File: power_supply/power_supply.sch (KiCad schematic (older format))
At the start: 50 parts, among them J1 Conn_01x04_Male, J2 Conn_01x03_Male, J3 Conn_01x03_Male, J4 Conn_01x03_Male, J5 Conn_01x02_Male, U1 LM7815_TO220, U2 LM7915_TO220, U3 LM7815_TO220

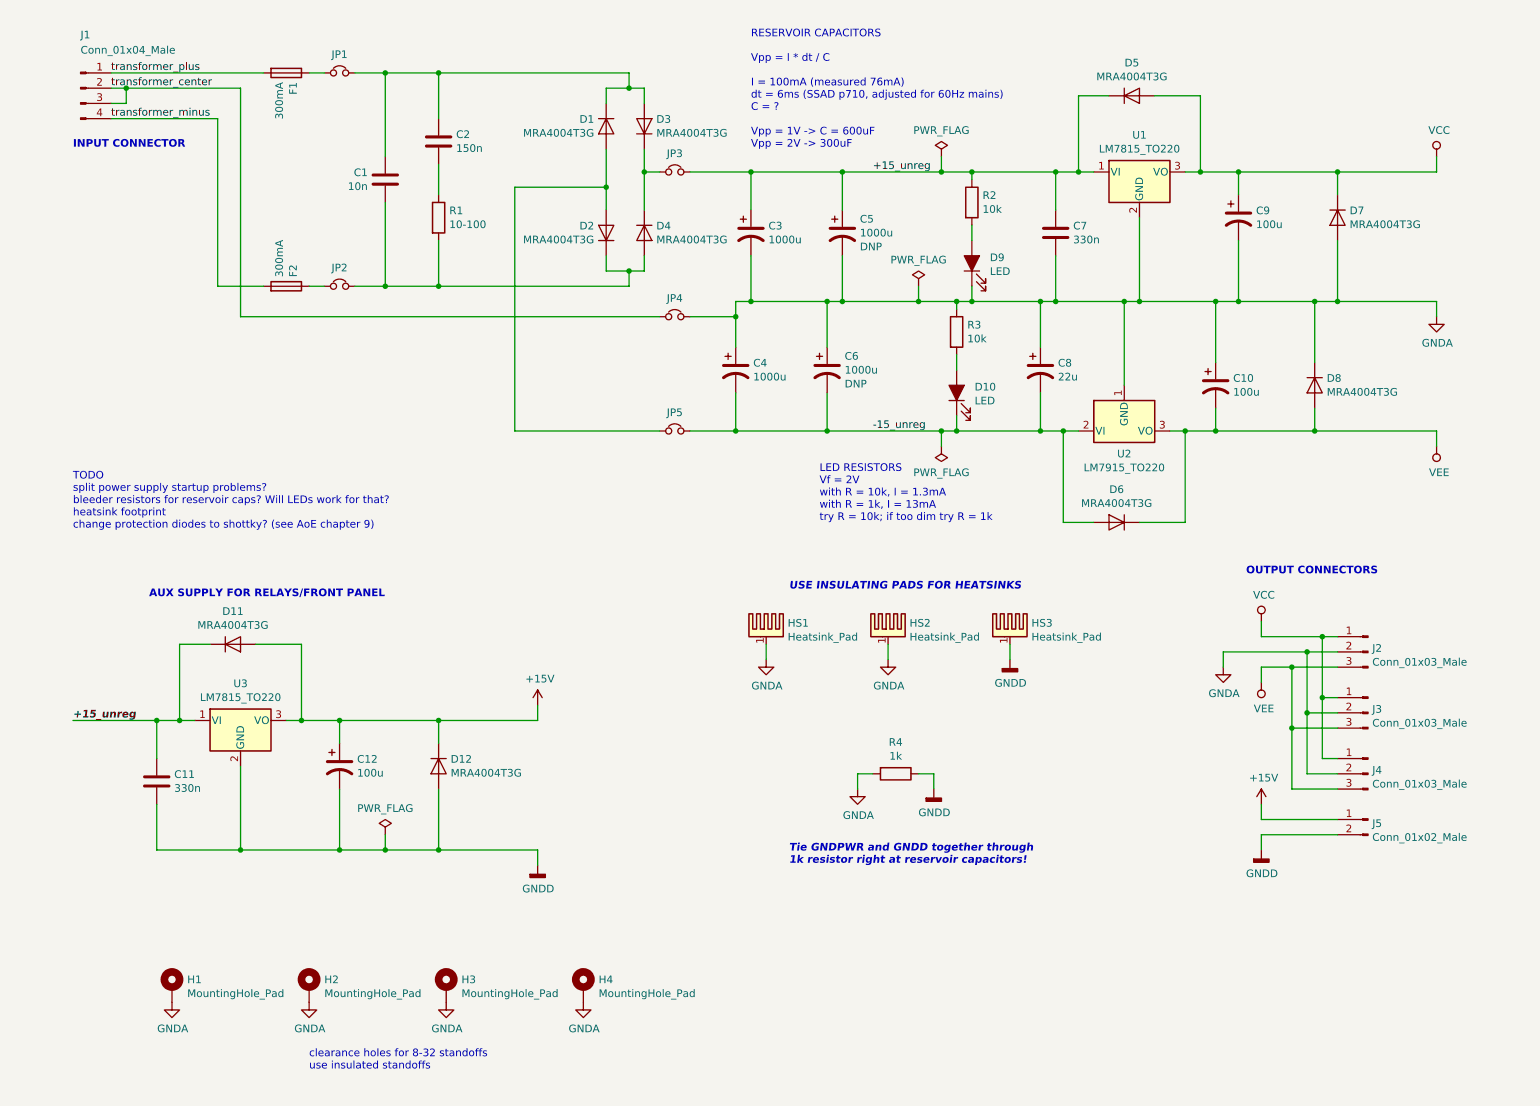
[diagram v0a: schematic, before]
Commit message: update power symbols (add relay power&ground)
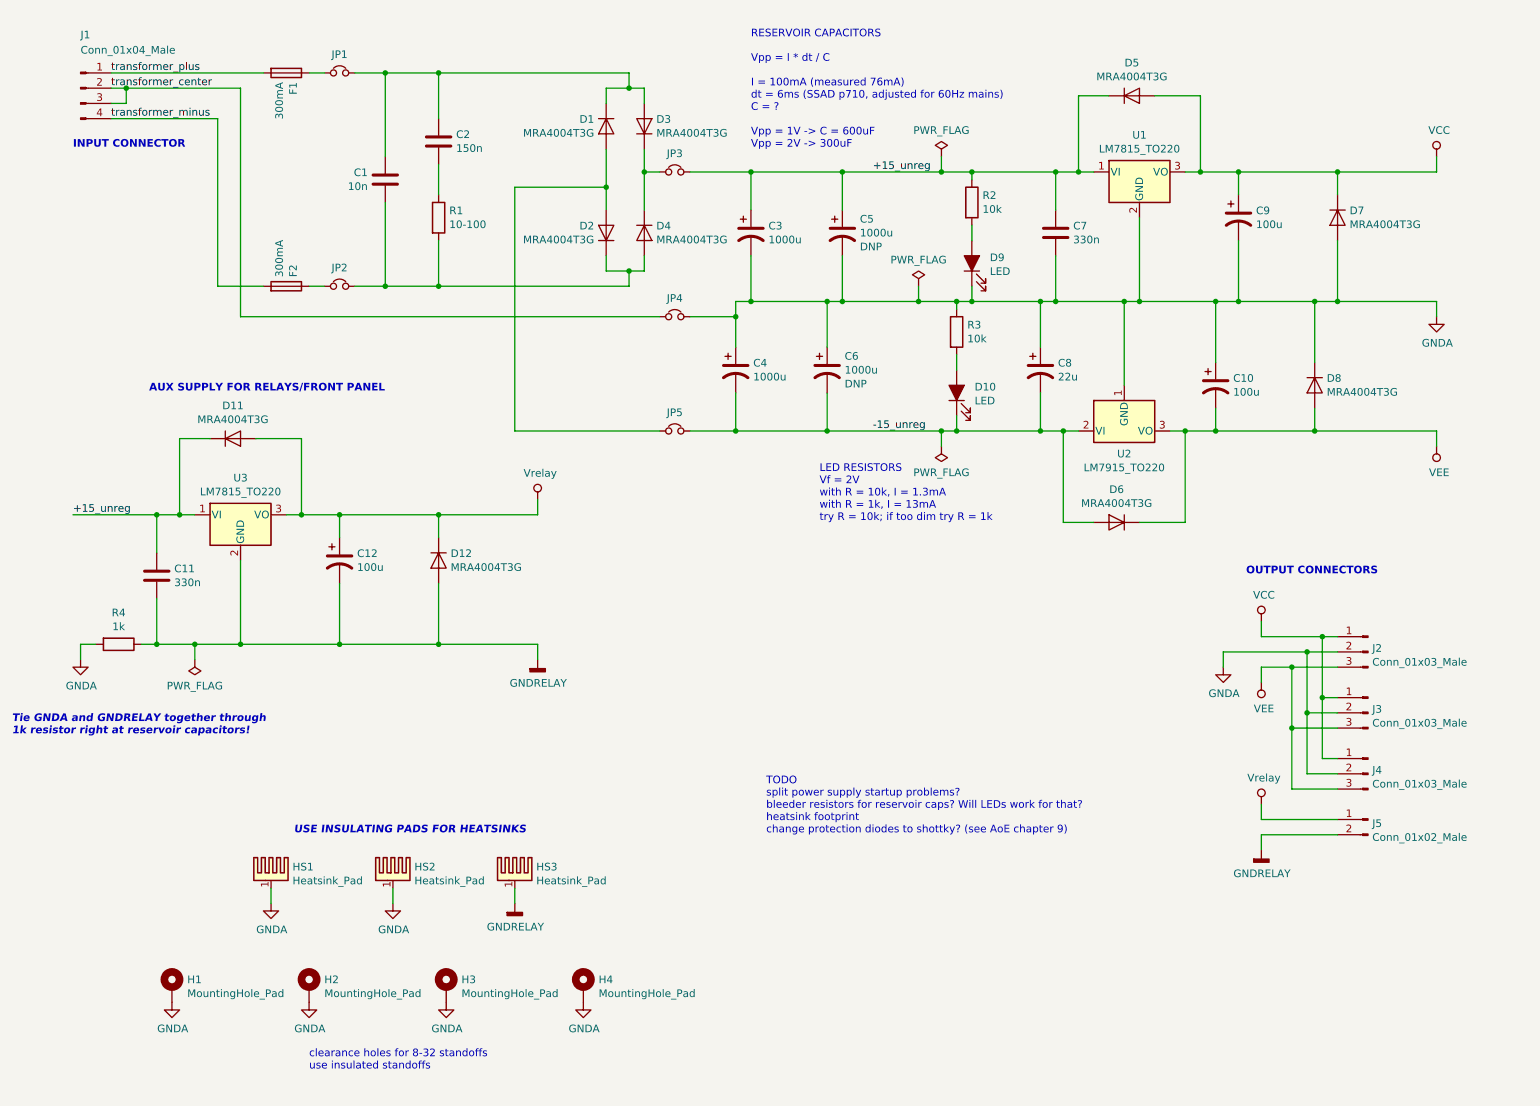
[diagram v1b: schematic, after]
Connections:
- net +15V renamed Vrelay
- net GNDD renamed GNDRELAY
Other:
- note added: "Tie GNDA and GNDRELAY together through\n1k resistor right at reservoir capacitors!"
- note removed: "Tie GNDPWR and GNDD together through\n1k resistor right at reservoir capacitors!"
- moved on the sheet: C11, C12, D11, D12, HS1, HS2, HS3, R4, U3

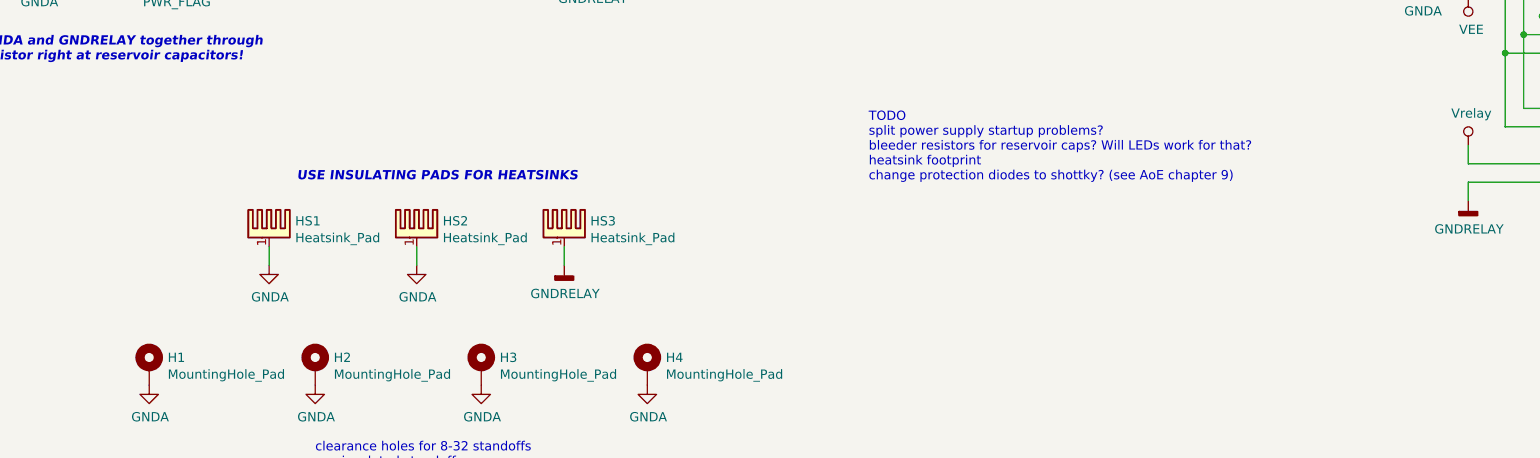
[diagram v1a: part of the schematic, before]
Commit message: update heatsinks in schematic
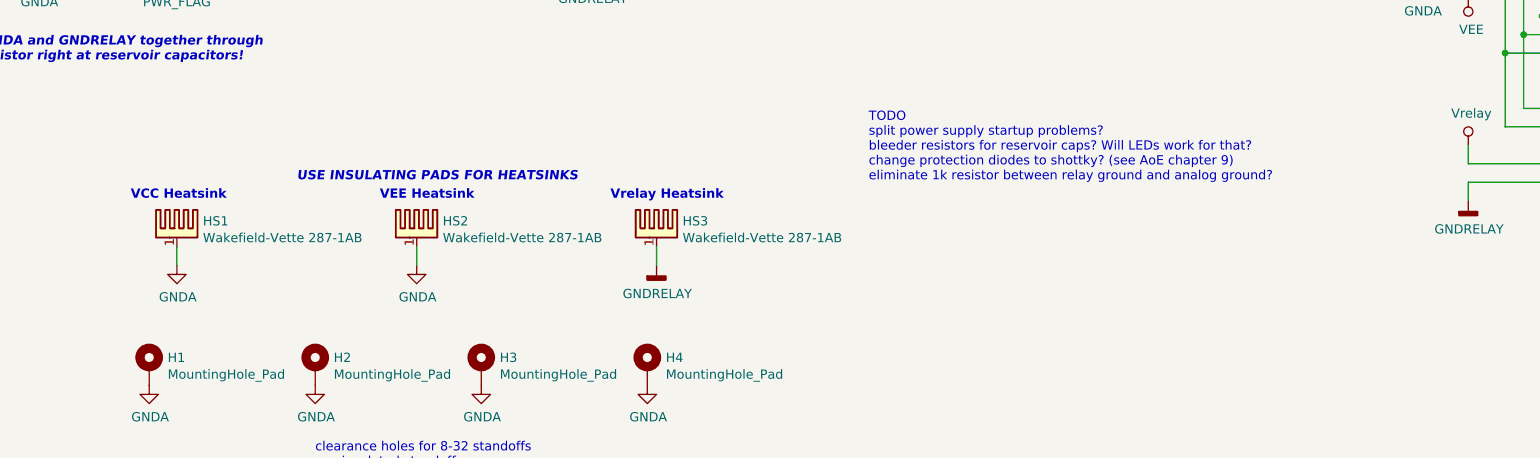
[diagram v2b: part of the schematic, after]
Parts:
- HS1, HS2, HS3: value Heatsink_Pad -> Wakefield-Vette 287-1AB; footprint Heatsink:Heatsink_35x26mm_1xFixation3mm_Fischer-SK486-35 -> Heatsink_gkeeth:Heatsink_Wakefield-Vette_287-1AB_T0-220_Vertical
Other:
- note added: "TODO\nsplit power supply startup problems?\nbleeder resistors for reservoir caps? Will LEDs work for that?\nchange protection diodes to shottky? (see AoE chapter 9)\neliminate 1k resistor between relay ground and analog ground?"
- note added: "VCC Heatsink"
- note added: "VEE Heatsink"
- note added: "Vrelay Heatsink"
- note removed: "TODO\nsplit power supply startup problems?\nbleeder resistors for reservoir caps? Will LEDs work for that?\nheatsink footprint\nchange protection diodes to shottky? (see AoE chapter 9)"
- moved on the sheet: HS1, HS3
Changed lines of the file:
@@
 $EndComp
 Text Notes 5500 6250 0    50   ~ 0
-TODO\nsplit power supply startup problems?\nbleeder resistors for reservoir caps? Will LEDs work for that?\nheatsink footprint\nchange protection diodes to shottky? (see AoE chapter 9)
+TODO\nsplit power supply startup problems?\nbleeder resistors for reservoir caps? Will LEDs work for that?\nchange protection diodes to shottky? (see AoE chapter 9)\neliminate 1k resistor between relay ground and analog ground?
 $Comp
 L Device:CP1 C8
@@
 $EndComp
 $Comp
-L Mechanical:Heatsink_Pad HS1
-U 1 1 5CB4FC2E
-P 2250 6500
-F 0 "HS1" H 2391 6539 50  0000 L CNN
-F 1 "Heatsink_Pad" H 2391 6448 50  0000 L CNN
-F 2 "Heatsink:Heatsink_35x26mm_1xFixation3mm_Fischer-SK486-35" H 2262 6450 50  0001 C CNN
-F 3 "~" H 2262 6450 50  0001 C CNN
-	1    2250 6500
-	1    0    0    -1
-$EndComp
-$Comp
 L Mechanical:Heatsink_Pad HS2
 U 1 1 5CB5054C
 P 3050 6500
 F 0 "HS2" H 3191 6539 50  0000 L CNN
-F 1 "Heatsink_Pad" H 3191 6448 50  0000 L CNN
-F 2 "Heatsink:Heatsink_35x26mm_1xFixation3mm_Fischer-SK486-35" H 3062 6450 50  0001 C CNN
+F 1 "Wakefield-Vette 287-1AB" H 3191 6448 50  0000 L CNN
+F 2 "Heatsink_gkeeth:Heatsink_Wakefield-Vette_287-1AB_T0-220_Vertical" H 3062 6450 50  0001 C CNN
 F 3 "~" H 3062 6450 50  0001 C CNN
 	1    3050 6500
@@
 Wire Wire Line
 	3050 6600 3050 6700
-Wire Wire Line
-	2250 6600 2250 6700
 Text Notes 2400 6250 0    50   Italic 10
 USE INSULATING PADS FOR HEATSINKS
@@
 	4000 4150 4000 4050
 $Comp
-L power:GNDA #PWR0106
-U 1 1 5CFBDF10
-P 2250 6700
-F 0 "#PWR0106" H 2250 6450 50  0001 C CNN
-F 1 "GNDA" H 2255 6527 50  0000 C CNN
-F 2 "" H 2250 6700 50  0001 C CNN
-F 3 "" H 2250 6700 50  0001 C CNN
-	1    2250 6700
-	1    0    0    -1
-$EndComp
-$Comp
 L power:GNDA #PWR0107
 U 1 1 5CFBE3DC
@@
 L Mechanical:Heatsink_Pad HS3
 U 1 1 5CFC037A
-P 3850 6500
-F 0 "HS3" H 3991 6539 50  0000 L CNN
-F 1 "Heatsink_Pad" H 3991 6448 50  0000 L CNN
-F 2 "Heatsink:Heatsink_35x26mm_1xFixation3mm_Fischer-SK486-35" H 3862 6450 50  0001 C CNN
-F 3 "~" H 3862 6450 50  0001 C CNN
-	1    3850 6500
-	1    0    0    -1
-$EndComp
-Wire Wire Line
-	3850 6600 3850 6700
+P 4350 6500
+F 0 "HS3" H 4491 6539 50  0000 L CNN
+F 1 "Wakefield-Vette 287-1AB" H 4491 6448 50  0000 L CNN
+F 2 "Heatsink_gkeeth:Heatsink_Wakefield-Vette_287-1AB_T0-220_Vertical" H 4362 6450 50  0001 C CNN
+F 3 "~" H 4362 6450 50  0001 C CNN
+	1    4350 6500
+	1    0    0    -1
+$EndComp
+Wire Wire Line
+	4350 6600 4350 6700
 $Comp
 L Connector:Conn_01x02_Male J5
@@
 L power_gkeeth:GNDRELAY #PWR0117
 U 1 1 5CCD5AC4
-P 3850 6700
-F 0 "#PWR0117" H 3850 6450 50  0001 C CNN
-F 1 "GNDRELAY" H 3854 6545 50  0000 C CNN
-F 2 "" H 3850 6700 50  0001 C CNN
-F 3 "" H 3850 6700 50  0001 C CNN
-	1    3850 6700
+P 4350 6700
+F 0 "#PWR0117" H 4350 6450 50  0001 C CNN
+F 1 "GNDRELAY" H 4354 6545 50  0000 C CNN
+F 2 "" H 4350 6700 50  0001 C CNN
+F 3 "" H 4350 6700 50  0001 C CNN
+	1    4350 6700
 	1    0    0    -1
 $EndComp
@@
 Wire Wire Line
 	1750 5000 1500 5000
+$Comp
+L power:GNDA #PWR0106
+U 1 1 5CFBDF10
+P 1750 6700
+F 0 "#PWR0106" H 1750 6450 50  0001 C CNN
+F 1 "GNDA" H 1755 6527 50  0000 C CNN
+F 2 "" H 1750 6700 50  0001 C CNN
+F 3 "" H 1750 6700 50  0001 C CNN
+	1    1750 6700
+	1    0    0    -1
+$EndComp
+Wire Wire Line
+	1750 6600 1750 6700
+$Comp
+L Mechanical:Heatsink_Pad HS1
+U 1 1 5CB4FC2E
+P 1750 6500
+F 0 "HS1" H 1891 6539 50  0000 L CNN
+F 1 "Wakefield-Vette 287-1AB" H 1891 6448 50  0000 L CNN
+F 2 "Heatsink_gkeeth:Heatsink_Wakefield-Vette_287-1AB_T0-220_Vertical" H 1762 6450 50  0001 C CNN
+F 3 "~" H 1762 6450 50  0001 C CNN
+	1    1750 6500
+	1    0    0    -1
+$EndComp
+Text Notes 1500 6350 0    50   ~ 10
+VCC Heatsink
+Text Notes 2850 6350 0    50   ~ 10
+VEE Heatsink
+Text Notes 4100 6350 0    50   ~ 10
+Vrelay Heatsink
 $EndSCHEMATC

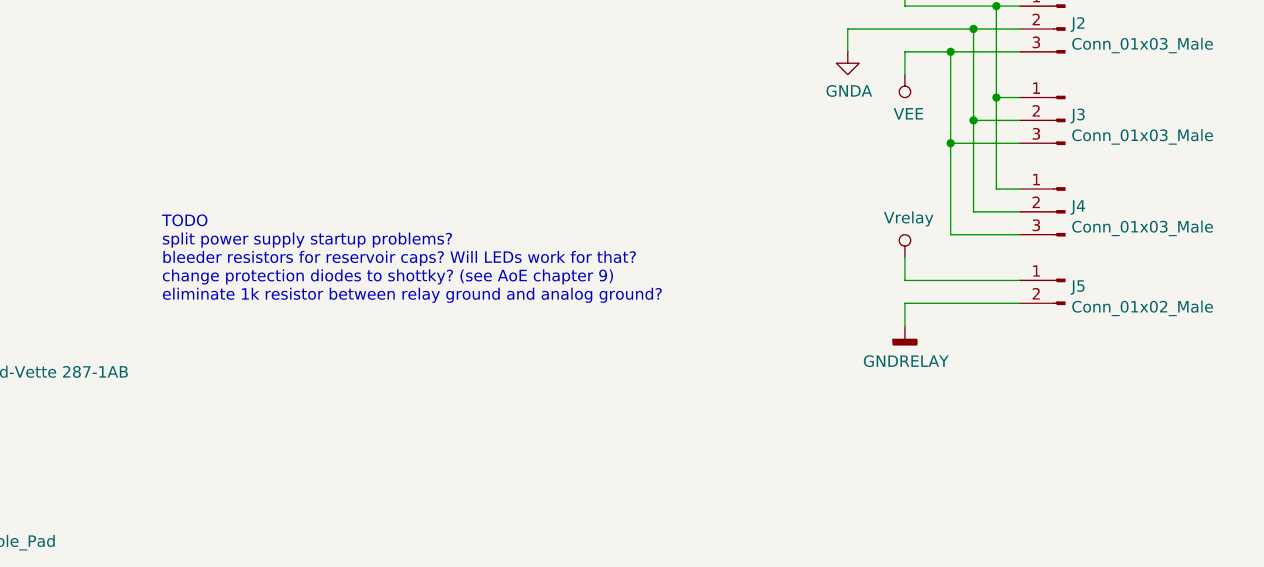
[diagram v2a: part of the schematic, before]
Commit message: update TODO and add extra connector for relay power
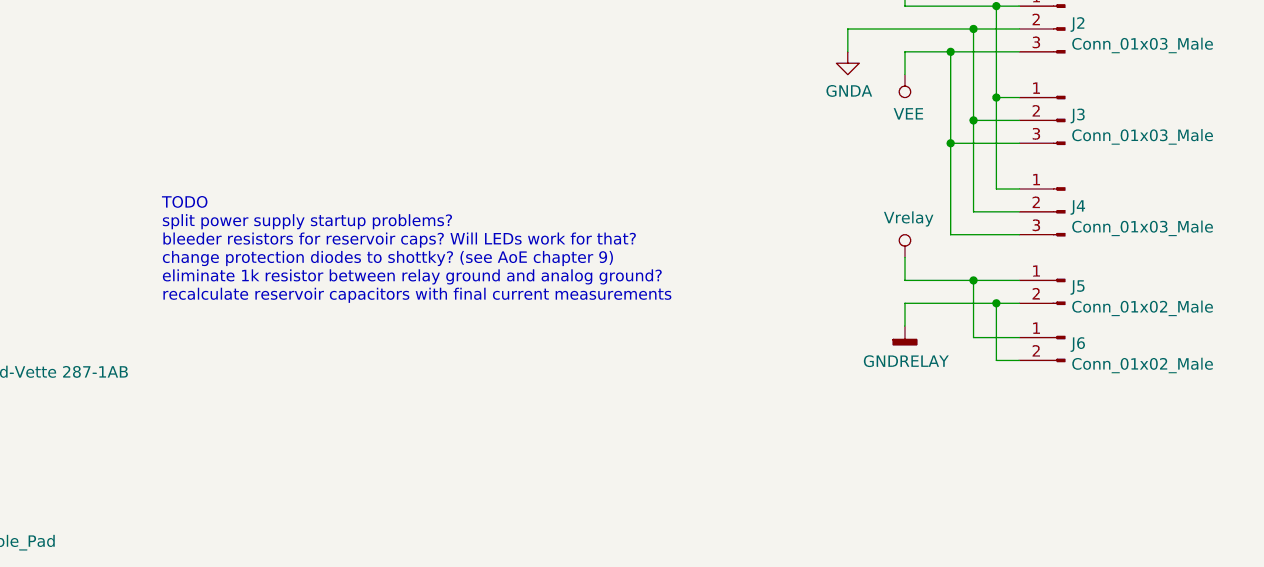
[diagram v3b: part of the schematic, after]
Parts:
- added J6: Conn_01x02_Male, Connector_Molex_SL:Molex_SL_A-70543-0001_1x02_P2.54mm_Vertical, symbol Connector:Conn_01x02_Male
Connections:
- net GNDRELAY: now also J6.2 (Pin_2)
- net Vrelay: now also J6.1 (Pin_1)
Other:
- note added: "TODO\nsplit power supply startup problems?\nbleeder resistors for reservoir caps? Will LEDs work for that?\nchange protection diodes to shottky? (see AoE chapter 9)\neliminate 1k resistor between relay ground and analog ground?\nrecalculate reservoir capacitors with final current measurements"
- note removed: "TODO\nsplit power supply startup problems?\nbleeder resistors for reservoir caps? Will LEDs work for that?\nchange protection diodes to shottky? (see AoE chapter 9)\neliminate 1k resistor between relay ground and analog ground?"
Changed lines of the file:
@@
 $EndComp
 Text Notes 5500 6250 0    50   ~ 0
-TODO\nsplit power supply startup problems?\nbleeder resistors for reservoir caps? Will LEDs work for that?\nchange protection diodes to shottky? (see AoE chapter 9)\neliminate 1k resistor between relay ground and analog ground?
+TODO\nsplit power supply startup problems?\nbleeder resistors for reservoir caps? Will LEDs work for that?\nchange protection diodes to shottky? (see AoE chapter 9)\neliminate 1k resistor between relay ground and analog ground?\nrecalculate reservoir capacitors with final current measurements
 $Comp
 L Device:CP1 C8
@@
 	8750 6050 8750 6150
 Wire Wire Line
-	8750 6150 9250 6150
+	8750 6150 9050 6150
 Wire Wire Line
 	8750 6350 8750 6250
 Wire Wire Line
-	8750 6250 9250 6250
+	8750 6250 9150 6250
 Text Notes 1450 3350 0    50   ~ 10
 AUX SUPPLY FOR RELAYS/FRONT PANEL
@@
 Text Notes 4100 6350 0    50   ~ 10
 Vrelay Heatsink
+$Comp
+L Connector:Conn_01x02_Male J6
+U 1 1 5D055D9A
+P 9450 6400
+F 0 "J6" H 9422 6374 50  0000 R CNN
+F 1 "Conn_01x02_Male" H 9422 6283 50  0000 R CNN
+F 2 "Connector_Molex_SL:Molex_SL_A-70543-0001_1x02_P2.54mm_Vertical" H 9450 6400 50  0001 C CNN
+F 3 "~" H 9450 6400 50  0001 C CNN
+	1    9450 6400
+	-1   0    0    -1
+$EndComp
+Wire Wire Line
+	9250 6400 9050 6400
+Wire Wire Line
+	9050 6400 9050 6150
+Connection ~ 9050 6150
+Wire Wire Line
+	9050 6150 9250 6150
+Wire Wire Line
+	9150 6250 9150 6500
+Wire Wire Line
+	9150 6500 9250 6500
+Connection ~ 9150 6250
+Wire Wire Line
+	9150 6250 9250 6250
 $EndSCHEMATC
